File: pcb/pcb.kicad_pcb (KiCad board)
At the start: 2 copper layers, 49 x 31 mm, 34 parts, among them J1 Conn_02x08_Odd_Even, J2 B2B-PH-K-S_LF__SN_, J3 USB_C_Receptacle, Q1 MMUN2211LT1G, SW1 SW_SPST, U1 TPS61090, U2 MCP73871-1AA

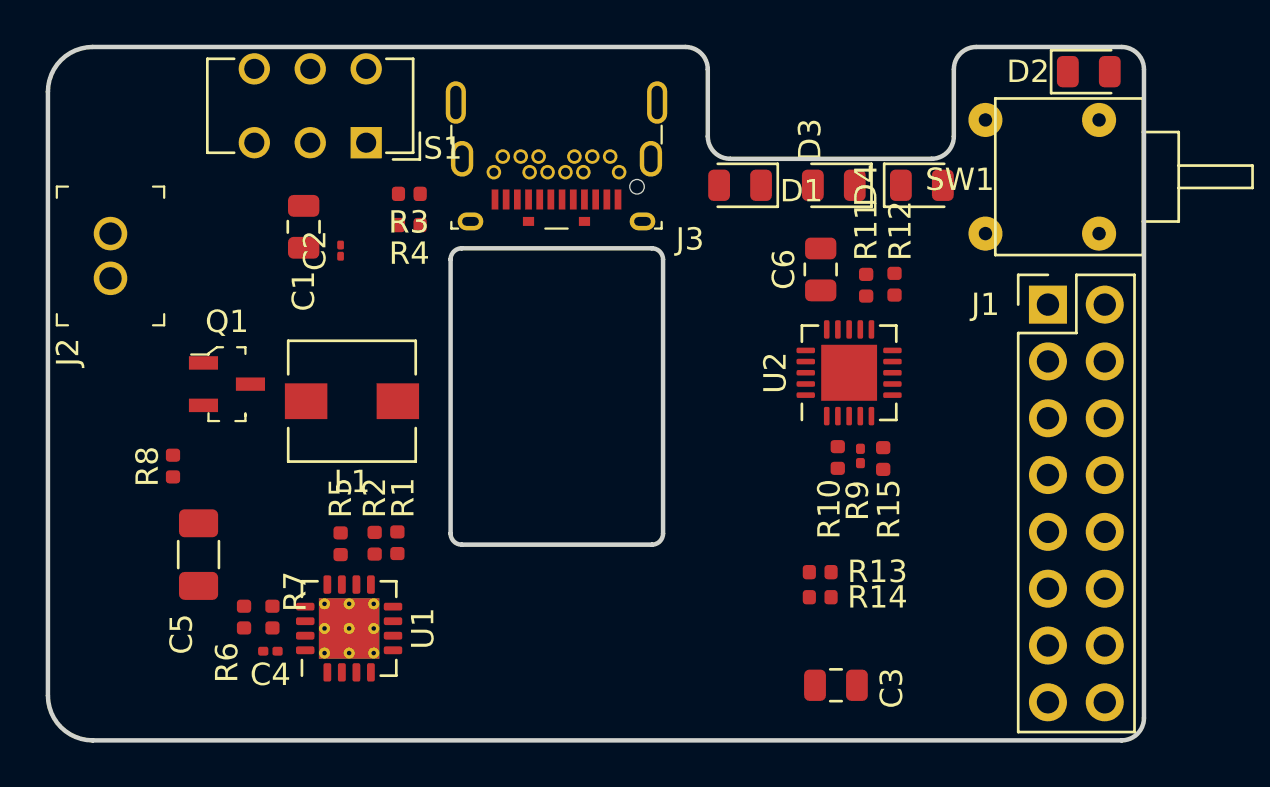
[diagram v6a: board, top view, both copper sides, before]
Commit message: updated cuts and placements, all 0805 SMD
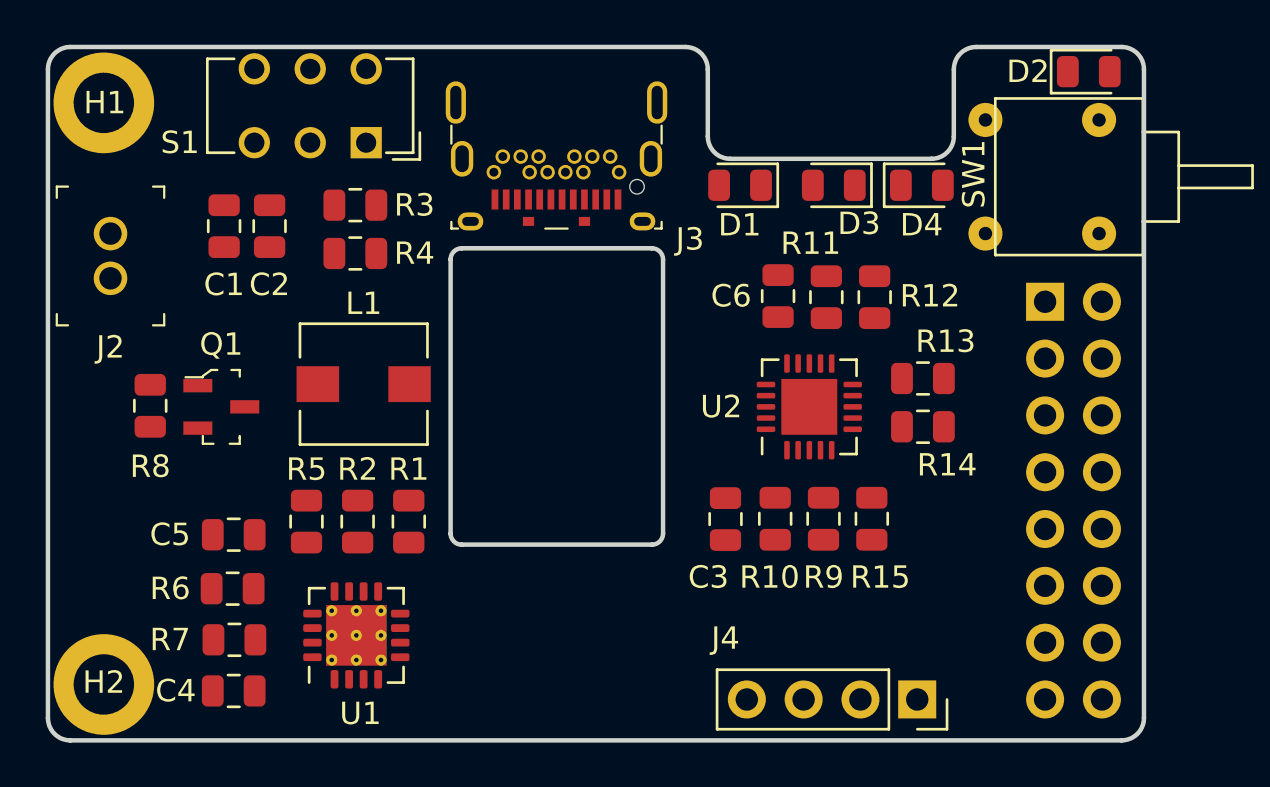
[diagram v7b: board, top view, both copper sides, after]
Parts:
- added H1: MountingHole, MountingHole:MountingHole_2.7mm_M2.5_ISO7380_Pad, F.Cu at (153.5, 71.5)
- added H2: MountingHole, MountingHole:MountingHole_2.7mm_M2.5_ISO7380_Pad, F.Cu at (153.5, 97.5)
- added J4: Conn_01x04, Connector_PinSocket_2.54mm:PinSocket_1x04_P2.54mm_Vertical, F.Cu at (189.9, 98.2)
- C2: footprint Capacitor_SMD:C_01005_0402Metric -> Capacitor_SMD:C_0805_2012Metric
- C4: footprint Capacitor_SMD:C_0201_0603Metric -> Capacitor_SMD:C_0805_2012Metric
- C5: footprint Capacitor_SMD:C_1206_3216Metric -> Capacitor_SMD:C_0805_2012Metric
- J1: footprint Connector_PinHeader_2.54mm:PinHeader_2x08_P2.54mm_Vertical -> Connector_PinSocket_2.54mm:PinSocket_2x08_P2.54mm_Vertical; moved to B.Cu
- R1, R10, R11, R12, R13, R14, R15, R2, R3, R4, R5, R6, R7, R8: footprint Resistor_SMD:R_0402_1005Metric -> Resistor_SMD:R_0805_2012Metric
- R9: footprint Resistor_SMD:R_0201_0603Metric -> Resistor_SMD:R_0805_2012Metric
- moved R13 9.80 mm to (190.1, 83.8)
- moved C3 8.92 mm to (181.3, 90.1), turned to 270 degrees
- moved R14 8.90 mm to (190.1, 86.0)
- moved R10 3.91 mm to (183.5, 90.1)
- moved C1 3.56 mm to (158.9, 77.0)
- moved C2 3.36 mm to (160.9, 77.0)
- moved R9 3.26 mm to (185.7, 90.1)
- moved R8 2.88 mm to (155.6, 85.0), turned to 90 degrees
- moved R15 2.74 mm to (187.8, 90.1)
- moved R4 2.73 mm to (164.7, 78.2)
- moved R3 2.47 mm to (164.7, 76.1)
- moved C4 2.42 mm to (159.3, 97.8)
- moved U2 2.34 mm to (185.0, 85.1)
- moved C6 2.25 mm to (183.6, 80.1)
- moved R7 1.98 mm to (159.3, 95.5), turned to 180 degrees
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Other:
- outline, holes or cut-outs redrawn

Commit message: updated pcb a little
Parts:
- moved U1 0.41 mm to (164.7, 95.7)
- moved C5 0.13 mm to (159.3, 90.9)
- moved D3 0.09 mm to (186.0, 75.2)
- moved R6 0.08 mm to (159.3, 93.2)
- moved C6 0.06 mm to (183.6, 80.2)
- turned D2 to 180 degrees
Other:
- board text added: "github.com/pvphan/tinycam"
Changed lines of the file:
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@@
   (general
     (thickness 1.6)
-    (drawings 40)
+    (drawings 41)
     (tracks 0)
     (zones 0)
@@
     (46 B.CrtYd user)
     (47 F.CrtYd user)
-    (48 B.Fab user)
-    (49 F.Fab user)
+    (48 B.Fab user hide)
+    (49 F.Fab user hide)
   )
   (setup
@@
     (descr "Through hole straight socket strip, 1x04, 2.54mm pitch, single row (from Kicad 4.0.7), script generated")
     (tags "Through hole socket strip THT 1x04 2.54mm single row")
-    (fp_text reference J4 (at -2.7305 8.5725 180) (layer F.SilkS)
+    (fp_text reference J4 (at -0.0635 10.668 180) (layer F.SilkS)
       (effects (font (size 1 1) (thickness 0.15)))
     )
@@
   )
   (module Resistor_SMD:R_0805_2012Metric (layer F.Cu)
-    (at 159.258 93.218)
+    (at 159.3365 93.218)
     (descr "Resistor SMD 0805 (2012 Metric), square (rectangular) end terminal, IPC_7351 nominal, (Body size source: https://docs.google.com/spreadsheets/d/1BsfQQcO9C6DZCsRaXUlFlo91Tg2WpOkGARC1WS5S8t0/edit?usp=sharing), generated with kicad-footprint-generator")
     (tags resistor)
@@
   )
   (module Capacitor_SMD:C_0805_2012Metric (layer F.Cu)
-    (at 159.3065 90.805)
+    (at 159.3365 90.932)
     (descr "Capacitor SMD 0805 (2012 Metric), square (rectangular) end terminal, IPC_7351 nominal, (Body size source: https://docs.google.com/spreadsheets/d/1BsfQQcO9C6DZCsRaXUlFlo91Tg2WpOkGARC1WS5S8t0/edit?usp=sharing), generated with kicad-footprint-generator")
     (tags capacitor)
@@
   )
   (module Capacitor_SMD:C_0805_2012Metric (layer F.Cu)
-    (at 183.642 80.137 90)
+    (at 183.642 80.2005 90)
     (descr "Capacitor SMD 0805 (2012 Metric), square (rectangular) end terminal, IPC_7351 nominal, (Body size source: https://docs.google.com/spreadsheets/d/1BsfQQcO9C6DZCsRaXUlFlo91Tg2WpOkGARC1WS5S8t0/edit?usp=sharing), generated with kicad-footprint-generator")
     (tags capacitor)
@@
   )
   (module LED_SMD:LED_0805_2012Metric (layer F.Cu)
-    (at 197.5335 70.104)
+    (at 197.5335 70.104 180)
     (descr "LED SMD 0805 (2012 Metric), square (rectangular) end terminal, IPC_7351 nominal, (Body size source: https://docs.google.com/spreadsheets/d/1BsfQQcO9C6DZCsRaXUlFlo91Tg2WpOkGARC1WS5S8t0/edit?usp=sharing), generated with kicad-footprint-generator")
     (tags diode)
     (attr smd)
-    (fp_text reference D2 (at -2.7155 0) (layer F.SilkS)
+    (fp_text reference D2 (at 2.906 -0.0635) (layer F.SilkS)
       (effects (font (size 1 1) (thickness 0.15)))
     )
@@
       (effects (font (size 0.5 0.5) (thickness 0.08)))
     )
-    (pad 2 smd roundrect (at 0.9375 0) (size 0.975 1.4) (layers F.Cu F.Paste F.Mask) (roundrect_rratio 0.25)
+    (pad 2 smd roundrect (at 0.9375 0 180) (size 0.975 1.4) (layers F.Cu F.Paste F.Mask) (roundrect_rratio 0.25)
       (net 4 5.0V))
-    (pad 1 smd roundrect (at -0.9375 0) (size 0.975 1.4) (layers F.Cu F.Paste F.Mask) (roundrect_rratio 0.25)
+    (pad 1 smd roundrect (at -0.9375 0 180) (size 0.975 1.4) (layers F.Cu F.Paste F.Mask) (roundrect_rratio 0.25)
       (net 1 GND))
     (model ${KISYS3DMOD}/LED_SMD.3dshapes/LED_0805_2012Metric.wrl
@@
   )
   (module LED_SMD:LED_0805_2012Metric (layer F.Cu)
-    (at 186.1335 75.184 180)
+    (at 186.04 75.184 180)
     (descr "LED SMD 0805 (2012 Metric), square (rectangular) end terminal, IPC_7351 nominal, (Body size source: https://docs.google.com/spreadsheets/d/1BsfQQcO9C6DZCsRaXUlFlo91Tg2WpOkGARC1WS5S8t0/edit?usp=sharing), generated with kicad-footprint-generator")
     (tags diode)
@@
   )
   (module Package_DFN_QFN:Texas_S-PVQFN-N16_EP2.7x2.7mm_ThermalVias (layer F.Cu)
-    (at 164.7885 95.306 90)
+    (at 164.6555 95.6945 90)
     (descr "QFN, 16 Pin (http://www.ti.com/lit/ds/symlink/msp430g2001.pdf#page=43), generated with kicad-footprint-generator ipc_noLead_generator.py")
     (tags "QFN NoLead")
@@
     )
   )
+  (gr_text github.com/pvphan/tinycam (at 180.2003 94.7928) (layer F.SilkS)
+    (effects (font (size 1 1) (thickness 0.16)))
+  )
   (gr_circle (center 198.22 80.44) (end 198.72 80.44) (layer Dwgs.User) (width 0.2))
